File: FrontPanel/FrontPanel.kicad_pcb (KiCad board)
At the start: 2 copper layers, 26 parts, among them SW11 Decimal, SW12 0, SW13 Backspace, SW14 Current 2, SW15 Cancel, SW21 1, SW22 2, SW23 3, SW24 Voltage 2, SW25 Confirm, SW31 4, SW32 5, SW33 6, SW34 Current 1, SW35 Channel 2, SW41 7, SW42 8, SW43 9, SW44 Voltage 1, SW45 Channel 1

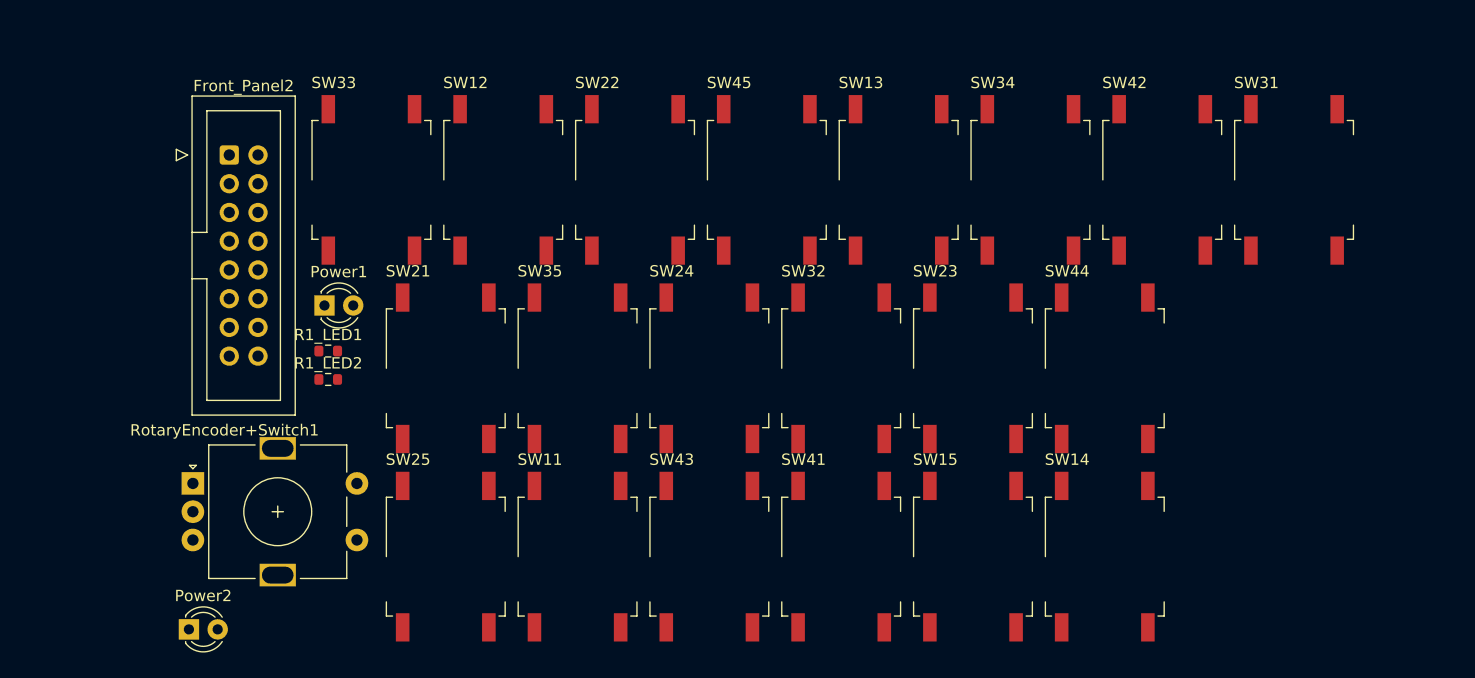
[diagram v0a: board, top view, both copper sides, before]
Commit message: Fixed button footprints
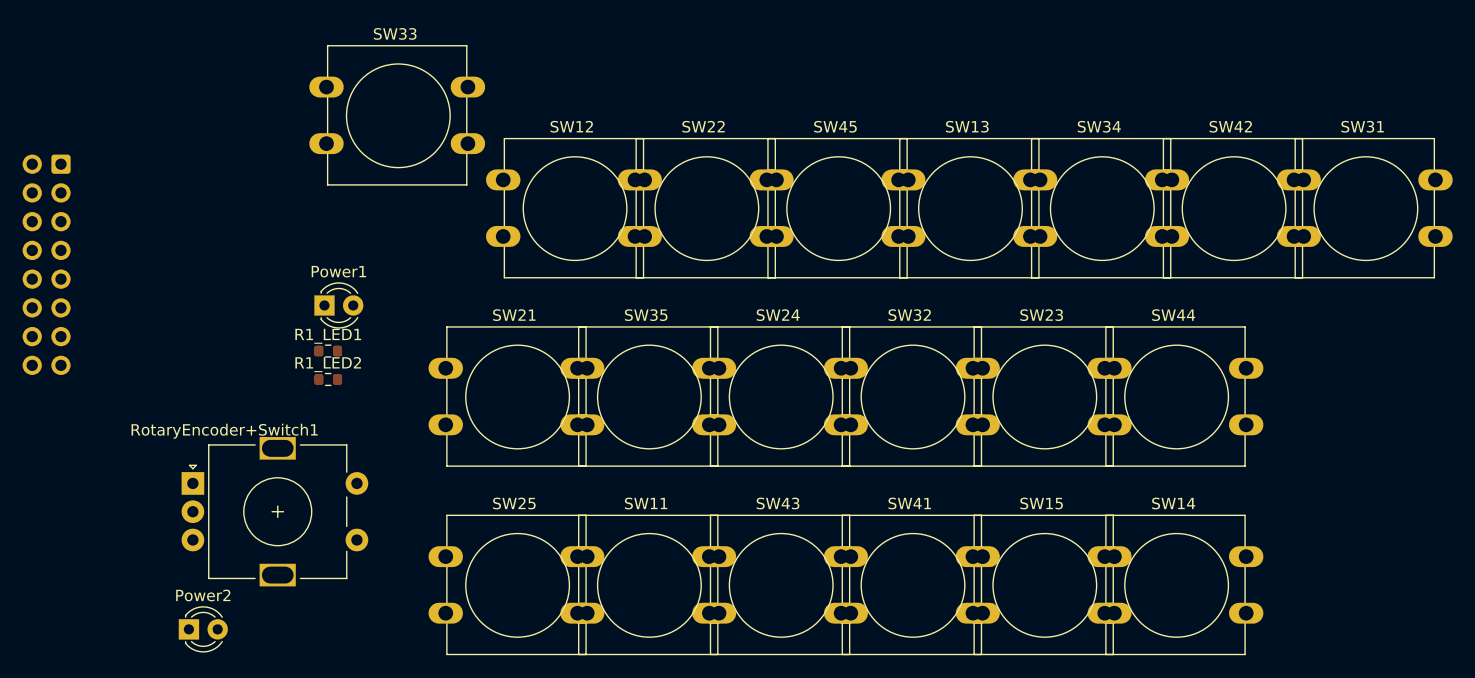
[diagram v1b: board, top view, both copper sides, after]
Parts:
- Front_Panel2: moved to B.Cu
- SW11, SW12, SW13, SW14, SW15, SW21, SW22, SW23, SW24, SW25, SW31, SW32, SW33, SW34, SW35, SW41, SW42, SW43, SW44, SW45: footprint Button_Switch_SMD:SW_MEC_5GSH9 -> Button_Switch_THT:SW_PUSH-12mm
- moved Front_Panel2 14.9 mm to (83.6, 68.3), turned to 180 degrees
- moved SW33 9.12 mm to (107.0, 61.5)

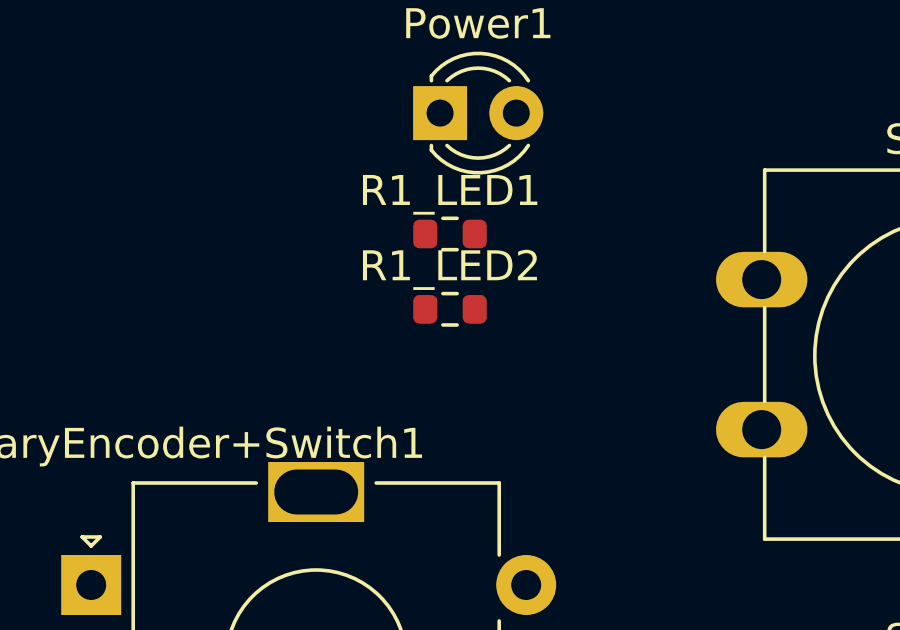
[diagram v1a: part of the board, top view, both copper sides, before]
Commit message: Remove/hide duplicate references, place values on silkscreen
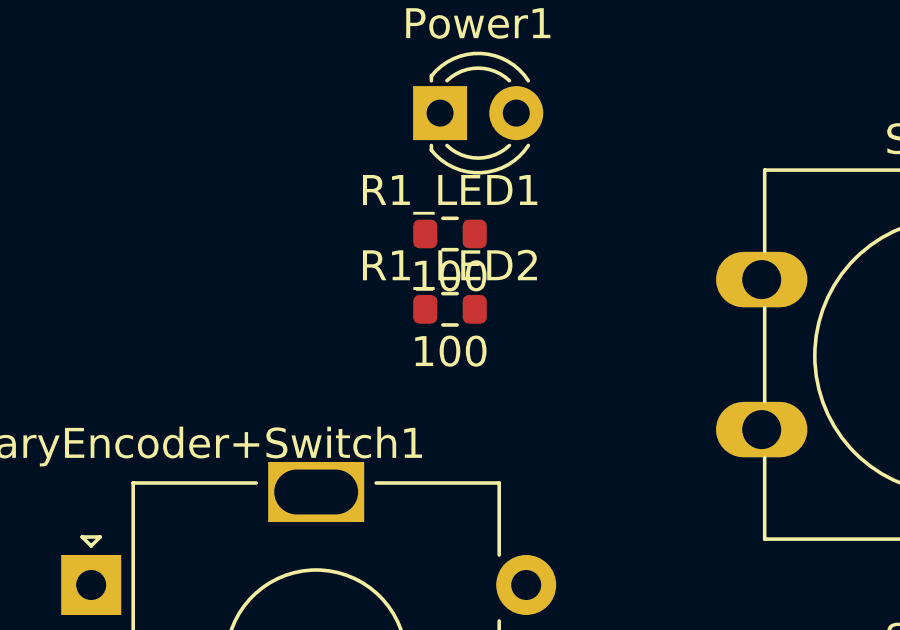
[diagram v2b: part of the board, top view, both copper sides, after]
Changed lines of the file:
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@@
       (effects (font (size 1 1) (thickness 0.15)))
     )
-    (fp_text value "4" (at 6.62 9.93) (layer "F.Fab")
-      (effects (font (size 1 1) (thickness 0.15)))
-    )
-    (fp_text user "${REFERENCE}" (at 6.35 2.54) (layer "F.Fab")
+    (fp_text value "4" (at 6.62 9.93) (layer "F.Fab") hide
       (effects (font (size 1 1) (thickness 0.15)))
     )
@@
       (effects (font (size 1 1) (thickness 0.15)))
     )
-    (fp_text value "Backspace" (at 6.62 9.93) (layer "F.Fab")
-      (effects (font (size 1 1) (thickness 0.15)))
-    )
-    (fp_text user "${REFERENCE}" (at 6.35 2.54) (layer "F.Fab")
+    (fp_text value "Backspace" (at 6.62 9.93) (layer "F.Fab") hide
       (effects (font (size 1 1) (thickness 0.15)))
     )
@@
       (effects (font (size 1 1) (thickness 0.15)))
     )
-    (fp_text value "100" (at 0 1.43) (layer "F.Fab")
-      (effects (font (size 1 1) (thickness 0.15)))
-    )
-    (fp_text user "${REFERENCE}" (at 0 0) (layer "F.Fab")
-      (effects (font (size 0.4 0.4) (thickness 0.06)))
+    (fp_text value "100" (at 0 1.43) (layer "F.SilkS")
+      (effects (font (size 1 1) (thickness 0.15)))
     )
     (fp_line (start -0.237258 0.5225) (end 0.237258 0.5225) (layer "F.SilkS") (width 0.12))
@@
       (effects (font (size 1 1) (thickness 0.15)))
     )
-    (fp_text value "Cancel" (at 6.62 9.93) (layer "F.Fab")
-      (effects (font (size 1 1) (thickness 0.15)))
-    )
-    (fp_text user "${REFERENCE}" (at 6.35 2.54) (layer "F.Fab")
+    (fp_text value "Cancel" (at 6.62 9.93) (layer "F.Fab") hide
       (effects (font (size 1 1) (thickness 0.15)))
     )
@@
       (effects (font (size 1 1) (thickness 0.15)))
     )
-    (fp_text value "100" (at 0 1.43) (layer "F.Fab")
-      (effects (font (size 1 1) (thickness 0.15)))
-    )
-    (fp_text user "${REFERENCE}" (at 0 0) (layer "F.Fab")
-      (effects (font (size 0.4 0.4) (thickness 0.06)))
+    (fp_text value "100" (at 0 1.43) (layer "F.SilkS")
+      (effects (font (size 1 1) (thickness 0.15)))
     )
     (fp_line (start -0.237258 -0.5225) (end 0.237258 -0.5225) (layer "F.SilkS") (width 0.12))
@@
       (effects (font (size 1 1) (thickness 0.15)))
     )
-    (fp_text value "Current 1" (at 6.62 9.93) (layer "F.Fab")
-      (effects (font (size 1 1) (thickness 0.15)))
-    )
-    (fp_text user "${REFERENCE}" (at 6.35 2.54) (layer "F.Fab")
+    (fp_text value "Current 1" (at 6.62 9.93) (layer "F.Fab") hide
       (effects (font (size 1 1) (thickness 0.15)))
     )
@@
       (effects (font (size 1 1) (thickness 0.15)))
     )
-    (fp_text value "6" (at 6.62 9.93) (layer "F.Fab")
-      (effects (font (size 1 1) (thickness 0.15)))
-    )
-    (fp_text user "${REFERENCE}" (at 6.35 2.54) (layer "F.Fab")
+    (fp_text value "6" (at 6.62 9.93) (layer "F.Fab") hide
       (effects (font (size 1 1) (thickness 0.15)))
     )
@@
       (effects (font (size 1 1) (thickness 0.15)))
     )
-    (fp_text value "Current 2" (at 6.62 9.93) (layer "F.Fab")
-      (effects (font (size 1 1) (thickness 0.15)))
-    )
-    (fp_text user "${REFERENCE}" (at 6.35 2.54) (layer "F.Fab")
+    (fp_text value "Current 2" (at 6.62 9.93) (layer "F.Fab") hide
       (effects (font (size 1 1) (thickness 0.15)))
     )
@@
       (effects (font (size 1 1) (thickness 0.15)))
     )
-    (fp_text value "Voltage 2" (at 6.62 9.93) (layer "F.Fab")
-      (effects (font (size 1 1) (thickness 0.15)))
-    )
-    (fp_text user "${REFERENCE}" (at 6.35 2.54) (layer "F.Fab")
+    (fp_text value "Voltage 2" (at 6.62 9.93) (layer "F.Fab") hide
       (effects (font (size 1 1) (thickness 0.15)))
     )
@@
       (effects (font (size 1 1) (thickness 0.15)))
     )
-    (fp_text value "LED" (at 1.27 2.96) (layer "F.Fab")
+    (fp_text value "LED" (at 1.27 2.96) (layer "F.Fab") hide
       (effects (font (size 1 1) (thickness 0.15)))
     )
@@
       (effects (font (size 1 1) (thickness 0.15)))
     )
-    (fp_text value "Channel 2" (at 6.62 9.93) (layer "F.Fab")
-      (effects (font (size 1 1) (thickness 0.15)))
-    )
-    (fp_text user "${REFERENCE}" (at 6.35 2.54) (layer "F.Fab")
+    (fp_text value "Channel 2" (at 6.62 9.93) (layer "F.Fab") hide
       (effects (font (size 1 1) (thickness 0.15)))
     )
@@
       (effects (font (size 1 1) (thickness 0.15)))
     )
-    (fp_text value "Confirm" (at 6.62 9.93) (layer "F.Fab")
-      (effects (font (size 1 1) (thickness 0.15)))
-    )
-    (fp_text user "${REFERENCE}" (at 6.35 2.54) (layer "F.Fab")
+    (fp_text value "Confirm" (at 6.62 9.93) (layer "F.Fab") hide
       (effects (font (size 1 1) (thickness 0.15)))
     )
@@
       (effects (font (size 1 1) (thickness 0.15)))
     )
-    (fp_text value "7" (at 6.62 9.93) (layer "F.Fab")
-      (effects (font (size 1 1) (thickness 0.15)))
-    )
-    (fp_text user "${REFERENCE}" (at 6.35 2.54) (layer "F.Fab")
+    (fp_text value "7" (at 6.62 9.93) (layer "F.Fab") hide
       (effects (font (size 1 1) (thickness 0.15)))
     )
@@
       (effects (font (size 1 1) (thickness 0.15)))
     )
-    (fp_text value "1" (at 6.62 9.93) (layer "F.Fab")
-      (effects (font (size 1 1) (thickness 0.15)))
-    )
-    (fp_text user "${REFERENCE}" (at 6.35 2.54) (layer "F.Fab")
+    (fp_text value "1" (at 6.62 9.93) (layer "F.Fab") hide
       (effects (font (size 1 1) (thickness 0.15)))
     )
@@
       (effects (font (size 1 1) (thickness 0.15)))
     )
-    (fp_text value "LED" (at 1.27 2.96) (layer "F.Fab")
+    (fp_text value "LED" (at 1.27 2.96) (layer "F.Fab") hide
       (effects (font (size 1 1) (thickness 0.15)))
     )
@@
       (effects (font (size 1 1) (thickness 0.15)))
     )
-    (fp_text value "Channel 1" (at 6.62 9.93) (layer "F.Fab")
-      (effects (font (size 1 1) (thickness 0.15)))
-    )
-    (fp_text user "${REFERENCE}" (at 6.35 2.54) (layer "F.Fab")
+    (fp_text value "Channel 1" (at 6.62 9.93) (layer "F.Fab") hide
       (effects (font (size 1 1) (thickness 0.15)))
     )
@@
       (effects (font (size 1 1) (thickness 0.15)))
     )
-    (fp_text value "3" (at 6.62 9.93) (layer "F.Fab")
-      (effects (font (size 1 1) (thickness 0.15)))
-    )
-    (fp_text user "${REFERENCE}" (at 6.35 2.54) (layer "F.Fab")
+    (fp_text value "3" (at 6.62 9.93) (layer "F.Fab") hide
       (effects (font (size 1 1) (thickness 0.15)))
     )
@@
       (effects (font (size 1 1) (thickness 0.15)))
     )
-    (fp_text value "IgnorePinsOnSymbol" (at 7.5 10.4) (layer "F.Fab")
-      (effects (font (size 1 1) (thickness 0.15)))
-    )
-    (fp_text user "${REFERENCE}" (at 11.1 6.3) (layer "F.Fab")
+    (fp_text value "IgnorePinsOnSymbol" (at 7.5 10.4) (layer "F.Fab") hide
       (effects (font (size 1 1) (thickness 0.15)))
     )
@@
       (effects (font (size 1 1) (thickness 0.15)))
     )
-    (fp_text value "Voltage 1" (at 6.62 9.93) (layer "F.Fab")
-      (effects (font (size 1 1) (thickness 0.15)))
-    )
-    (fp_text user "${REFERENCE}" (at 6.35 2.54) (layer "F.Fab")
+    (fp_text value "Voltage 1" (at 6.62 9.93) (layer "F.Fab") hide
       (effects (font (size 1 1) (thickness 0.15)))
     )
@@
       (effects (font (size 1 1) (thickness 0.15)))
     )
-    (fp_text value "0" (at 6.62 9.93) (layer "F.Fab")
-      (effects (font (size 1 1) (thickness 0.15)))
-    )
-    (fp_text user "${REFERENCE}" (at 6.35 2.54) (layer "F.Fab")
+    (fp_text value "0" (at 6.62 9.93) (layer "F.Fab") hide
       (effects (font (size 1 1) (thickness 0.15)))
     )
@@
       (effects (font (size 1 1) (thickness 0.15)))
     )
-    (fp_text value "8" (at 6.62 9.93) (layer "F.Fab")
-      (effects (font (size 1 1) (thickness 0.15)))
-    )
-    (fp_text user "${REFERENCE}" (at 6.35 2.54) (layer "F.Fab")
+    (fp_text value "8" (at 6.62 9.93) (layer "F.Fab") hide
       (effects (font (size 1 1) (thickness 0.15)))
     )
@@
       (effects (font (size 1 1) (thickness 0.15)))
     )
-    (fp_text value "9" (at 6.62 9.93) (layer "F.Fab")
-      (effects (font (size 1 1) (thickness 0.15)))
-    )
-    (fp_text user "${REFERENCE}" (at 6.35 2.54) (layer "F.Fab")
+    (fp_text value "9" (at 6.62 9.93) (layer "F.Fab") hide
       (effects (font (size 1 1) (thickness 0.15)))
     )
@@
       (effects (font (size 1 1) (thickness 0.15)))
     )
-    (fp_text value "2" (at 6.62 9.93) (layer "F.Fab")
-      (effects (font (size 1 1) (thickness 0.15)))
-    )
-    (fp_text user "${REFERENCE}" (at 6.35 2.54) (layer "F.Fab")
+    (fp_text value "2" (at 6.62 9.93) (layer "F.Fab") hide
       (effects (font (size 1 1) (thickness 0.15)))
     )
@@
       (effects (font (size 1 1) (thickness 0.15)))
     )
-    (fp_text value "Decimal" (at 6.62 9.93) (layer "F.Fab")
-      (effects (font (size 1 1) (thickness 0.15)))
-    )
-    (fp_text user "${REFERENCE}" (at 6.35 2.54) (layer "F.Fab")
+    (fp_text value "Decimal" (at 6.62 9.93) (layer "F.Fab") hide
       (effects (font (size 1 1) (thickness 0.15)))
     )
@@
       (effects (font (size 1 1) (thickness 0.15)))
     )
-    (fp_text value "5" (at 6.62 9.93) (layer "F.Fab")
-      (effects (font (size 1 1) (thickness 0.15)))
-    )
-    (fp_text user "${REFERENCE}" (at 6.35 2.54) (layer "F.Fab")
+    (fp_text value "5" (at 6.62 9.93) (layer "F.Fab") hide
       (effects (font (size 1 1) (thickness 0.15)))
     )
@@
       (effects (font (size 1 1) (thickness 0.15)) (justify mirror))
     )
-    (fp_text value "Conn_02x08_Counter_Clockwise" (at 1.27 -23.88) (layer "B.Fab")
+    (fp_text value "Conn_02x08_Counter_Clockwise" (at 1.27 -23.88) (layer "B.Fab") hide
       (effects (font (size 1 1) (thickness 0.15)) (justify mirror))
     )
-    (fp_text user "${REFERENCE}" (at 1.27 -8.89 90) (layer "B.Fab")
-      (effects (font (size 1 1) (thickness 0.15)) (justify mirror))
-    )

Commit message: Grouped up keypad
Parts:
- removed SW21: 1, Button_Switch_THT:SW_PUSH-12mm
- removed SW22: 2, Button_Switch_THT:SW_PUSH-12mm
- removed SW23: 3, Button_Switch_THT:SW_PUSH-12mm
- removed SW24: Voltage 2, Button_Switch_THT:SW_PUSH-12mm
- removed SW25: Confirm, Button_Switch_THT:SW_PUSH-12mm
- removed SW31: 4, Button_Switch_THT:SW_PUSH-12mm
- removed SW32: 5, Button_Switch_THT:SW_PUSH-12mm
- removed SW33: 6, Button_Switch_THT:SW_PUSH-12mm
- removed SW34: Current 1, Button_Switch_THT:SW_PUSH-12mm
- removed SW35: Channel 2, Button_Switch_THT:SW_PUSH-12mm
- removed SW41: 7, Button_Switch_THT:SW_PUSH-12mm
- removed SW42: 8, Button_Switch_THT:SW_PUSH-12mm
- removed SW43: 9, Button_Switch_THT:SW_PUSH-12mm
- removed SW44: Voltage 1, Button_Switch_THT:SW_PUSH-12mm
- removed SW45: Channel 1, Button_Switch_THT:SW_PUSH-12mm
- added C_DBC_1: 100n, Capacitor_SMD:C_0603_1608Metric, F.Cu at (198.1, 30.0)
- added C_DBC_10: 100n, Capacitor_SMD:C_0603_1608Metric, F.Cu at (237.7, 47.8)
- added C_DBC_11: 100n, Capacitor_SMD:C_0603_1608Metric, F.Cu at (237.7, 65.5)
- added C_DBC_12: 100n, Capacitor_SMD:C_0603_1608Metric, F.Cu at (237.7, 83.3)
- added C_DBC_13: 100n, Capacitor_SMD:C_0603_1608Metric, F.Cu at (257.6, 30.0)
- added C_DBC_14: 100n, Capacitor_SMD:C_0603_1608Metric, F.Cu at (257.6, 47.8)
- added C_DBC_15: 100n, Capacitor_SMD:C_0603_1608Metric, F.Cu at (257.6, 65.5)
- added C_DBC_16: 100n, Capacitor_SMD:C_0603_1608Metric, F.Cu at (257.6, 83.3)
- added C_DBC_17: 100n, Capacitor_SMD:C_0603_1608Metric, F.Cu at (277.4, 30.0)
- added C_DBC_18: 100n, Capacitor_SMD:C_0603_1608Metric, F.Cu at (277.4, 47.8)
- added C_DBC_19: 100n, Capacitor_SMD:C_0603_1608Metric, F.Cu at (277.4, 65.5)
- added C_DBC_2: 100n, Capacitor_SMD:C_0603_1608Metric, F.Cu at (198.1, 47.8)
- added C_DBC_20: 100n, Capacitor_SMD:C_0603_1608Metric, F.Cu at (277.4, 83.3)
- added C_DBC_3: 100n, Capacitor_SMD:C_0603_1608Metric, F.Cu at (198.1, 65.5)
- added C_DBC_4: 100n, Capacitor_SMD:C_0603_1608Metric, F.Cu at (198.1, 83.3)
- added C_DBC_5: 100n, Capacitor_SMD:C_0603_1608Metric, F.Cu at (217.9, 30.0)
- added C_DBC_6: 100n, Capacitor_SMD:C_0603_1608Metric, F.Cu at (217.9, 47.8)
- added C_DBC_7: 100n, Capacitor_SMD:C_0603_1608Metric, F.Cu at (217.9, 65.5)
- added C_DBC_8: 100n, Capacitor_SMD:C_0603_1608Metric, F.Cu at (217.9, 83.3)
- added C_DBC_9: 100n, Capacitor_SMD:C_0603_1608Metric, F.Cu at (237.7, 30.0)
- added R_DBC_1: 1k, Resistor_SMD:R_0603_1608Metric, F.Cu at (200.7, 30.0)
- added R_DBC_10: 1k, Resistor_SMD:R_0603_1608Metric, F.Cu at (240.3, 47.8)
- added R_DBC_11: 1k, Resistor_SMD:R_0603_1608Metric, F.Cu at (240.3, 65.5)
- added R_DBC_12: 1k, Resistor_SMD:R_0603_1608Metric, F.Cu at (240.3, 83.3)
- added R_DBC_13: 1k, Resistor_SMD:R_0603_1608Metric, F.Cu at (260.1, 30.0)
- added R_DBC_14: 1k, Resistor_SMD:R_0603_1608Metric, F.Cu at (260.1, 47.8)
- added R_DBC_15: 1k, Resistor_SMD:R_0603_1608Metric, F.Cu at (260.1, 65.5)
- added R_DBC_16: 1k, Resistor_SMD:R_0603_1608Metric, F.Cu at (260.1, 83.3)
- added R_DBC_17: 1k, Resistor_SMD:R_0603_1608Metric, F.Cu at (279.9, 30.0)
- added R_DBC_18: 1k, Resistor_SMD:R_0603_1608Metric, F.Cu at (279.9, 47.8)
- added R_DBC_19: 1k, Resistor_SMD:R_0603_1608Metric, F.Cu at (279.9, 65.5)
- added R_DBC_2: 1k, Resistor_SMD:R_0603_1608Metric, F.Cu at (200.7, 47.8)
- added R_DBC_20: 1k, Resistor_SMD:R_0603_1608Metric, F.Cu at (279.9, 83.3)
- added R_DBC_3: 1k, Resistor_SMD:R_0603_1608Metric, F.Cu at (200.7, 65.5)
- added R_DBC_4: 1k, Resistor_SMD:R_0603_1608Metric, F.Cu at (200.7, 83.3)
- added R_DBC_5: 1k, Resistor_SMD:R_0603_1608Metric, F.Cu at (220.5, 30.0)
- added R_DBC_6: 1k, Resistor_SMD:R_0603_1608Metric, F.Cu at (220.5, 47.8)
- added R_DBC_7: 1k, Resistor_SMD:R_0603_1608Metric, F.Cu at (220.5, 65.5)
- added R_DBC_8: 1k, Resistor_SMD:R_0603_1608Metric, F.Cu at (220.5, 83.3)
- added R_DBC_9: 1k, Resistor_SMD:R_0603_1608Metric, F.Cu at (240.3, 30.0)
- added SW1: Channel 1, Button_Switch_THT:SW_PUSH-12mm, F.Cu at (187.0, 30.1)
- added SW10: 5, Button_Switch_THT:SW_PUSH-12mm, F.Cu at (226.6, 47.9)
- added SW16: Backspace, Button_Switch_THT:SW_PUSH-12mm, F.Cu at (246.4, 83.5)
- added SW17: Voltage 1, Button_Switch_THT:SW_PUSH-12mm, F.Cu at (266.2, 30.1)
- added SW18: Current 1, Button_Switch_THT:SW_PUSH-12mm, F.Cu at (266.2, 47.9)
- added SW19: Voltage 2, Button_Switch_THT:SW_PUSH-12mm, F.Cu at (266.2, 65.7)
- added SW2: Confirm, Button_Switch_THT:SW_PUSH-12mm, F.Cu at (187.0, 47.9)
- added SW20: Current 2, Button_Switch_THT:SW_PUSH-12mm, F.Cu at (266.2, 83.5)
- added SW3: Cancel, Button_Switch_THT:SW_PUSH-12mm, F.Cu at (187.0, 65.7)
- added SW4: Channel 2, Button_Switch_THT:SW_PUSH-12mm, F.Cu at (187.0, 83.5)
- added SW5: 7, Button_Switch_THT:SW_PUSH-12mm, F.Cu at (206.8, 30.1)
- added SW6: 4, Button_Switch_THT:SW_PUSH-12mm, F.Cu at (206.8, 47.9)
- added SW7: 1, Button_Switch_THT:SW_PUSH-12mm, F.Cu at (206.8, 65.7)
- added SW8: Decimal, Button_Switch_THT:SW_PUSH-12mm, F.Cu at (206.8, 83.5)
- added SW9: 8, Button_Switch_THT:SW_PUSH-12mm, F.Cu at (226.6, 30.1)
- SW11: value Decimal -> 2
- SW13: value Backspace -> 9
- SW14: value Current 2 -> 6
- SW15: value Cancel -> 3
- moved SW12 104.8 mm to (226.6, 83.5), turned to 90 degrees
- moved SW11 104.3 mm to (226.6, 65.7), turned to 90 degrees
- moved SW13 97.2 mm to (246.4, 30.1), turned to 90 degrees
- moved SW15 90.3 mm to (246.4, 65.7), turned to 90 degrees
- moved SW14 89.6 mm to (246.4, 47.9), turned to 90 degrees
- moved Front_Panel2 78.8 mm to (20.3, 21.3)
- moved Power2 78.8 mm to (31.6, 62.5)
- moved R1_LED1 78.8 mm to (43.9, 37.9)
- moved R1_LED2 78.8 mm to (43.9, 40.4)
- moved RotaryEncoder+Switch1 78.8 mm to (32.0, 49.6)
- moved Power1 78.8 mm to (43.6, 33.8)
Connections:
- SW11 pad 1: Net-(Front_Panel2-Pad11) -> Net-(Front_Panel2-Pad9)
- SW11 pad 2: Net-(Front_Panel2-Pad11) -> Net-(Front_Panel2-Pad14)
- SW12 pad 1: Net-(Front_Panel2-Pad11) -> Net-(Front_Panel2-Pad8)
- SW12 pad 2: Net-(Front_Panel2-Pad11) -> Net-(Front_Panel2-Pad14)
- SW13 pad 2: Net-(Front_Panel2-Pad11) -> Net-(Front_Panel2-Pad13)
- SW14 pad 1: Net-(Front_Panel2-Pad11) -> Net-(Front_Panel2-Pad10)
- SW14 pad 2: Net-(Front_Panel2-Pad11) -> Net-(Front_Panel2-Pad13)
- SW15 pad 1: Net-(Front_Panel2-Pad11) -> Net-(Front_Panel2-Pad9)
- SW15 pad 2: Net-(Front_Panel2-Pad11) -> Net-(Front_Panel2-Pad13)
